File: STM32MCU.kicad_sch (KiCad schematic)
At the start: 17 parts, among them J7 Conn_02x05_Odd_Even, SW1 SW_Push, U4 STM32C542CCT6, Y1 ECS-120-18-33-JGN-TR

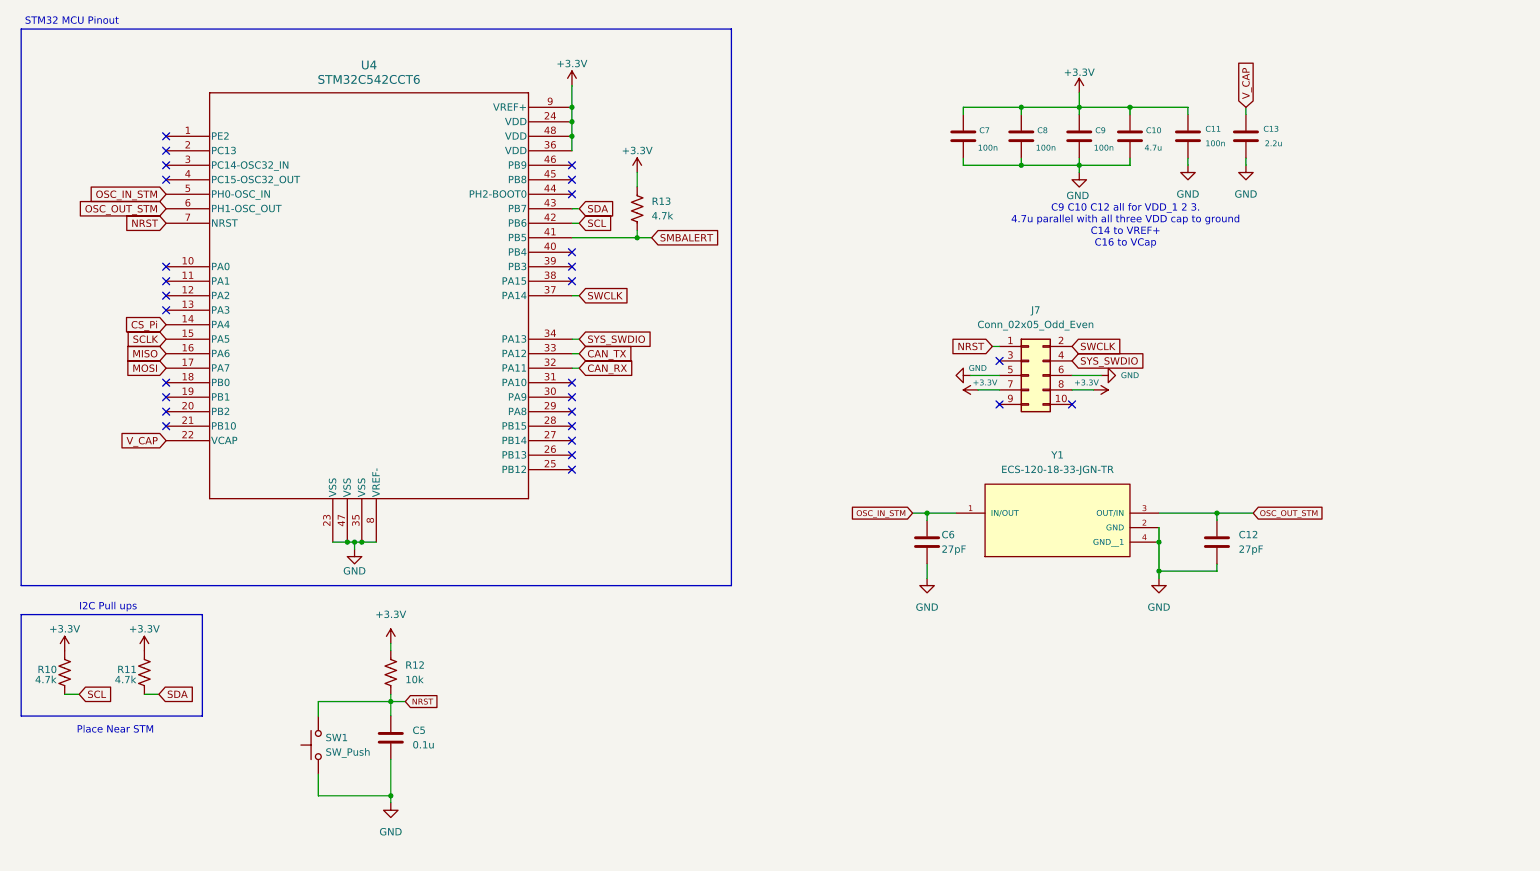
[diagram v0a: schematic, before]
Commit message: Split SMBALERT pins and added pull-up resistors
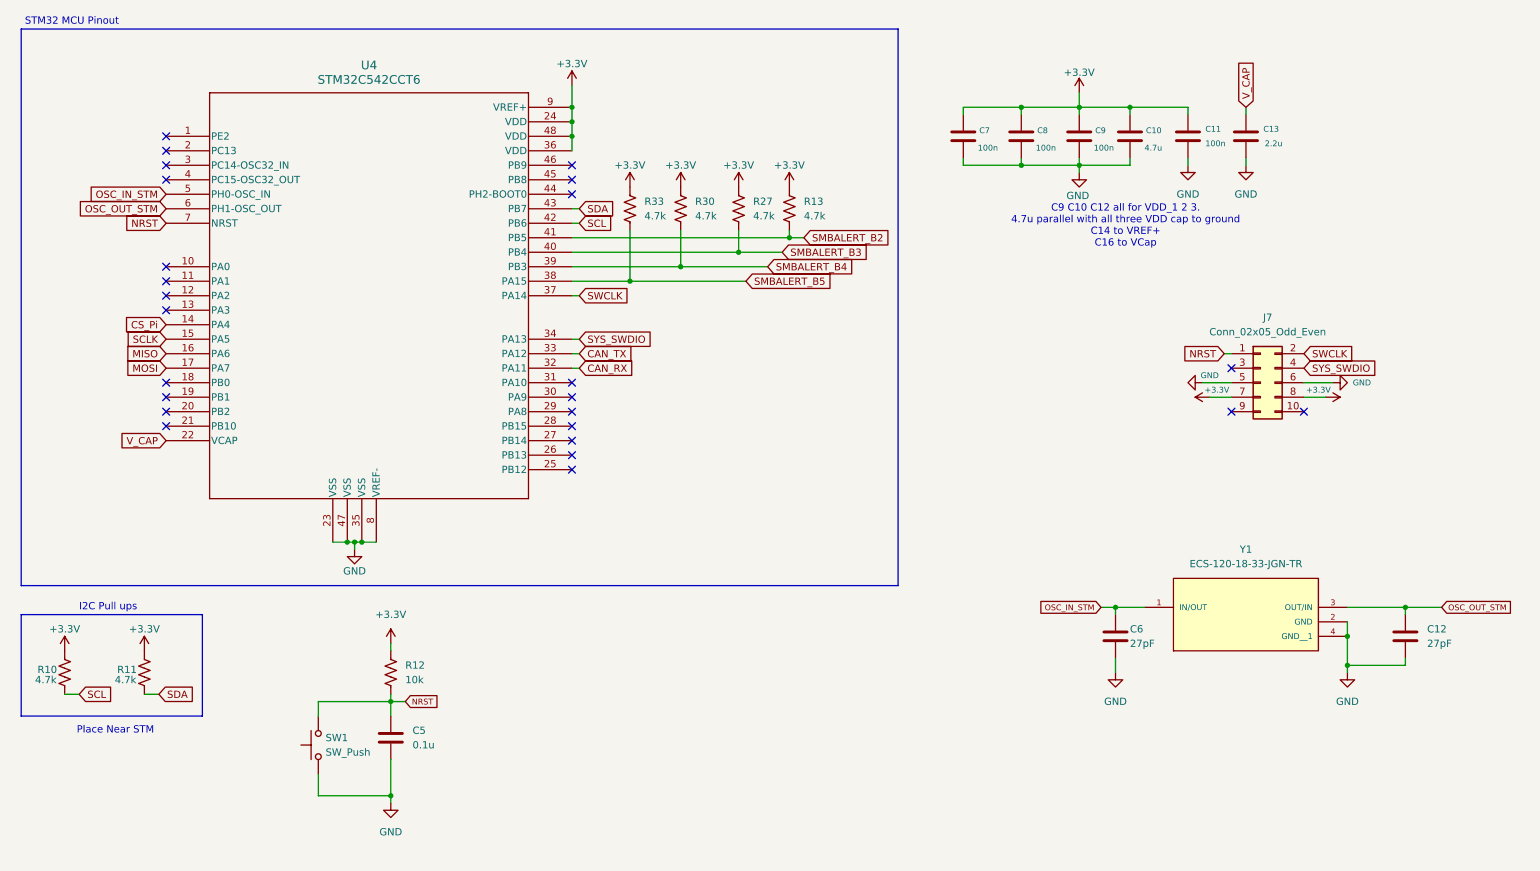
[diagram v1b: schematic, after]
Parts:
- added R27, R30, R33: 4.7k, E48SC12030NRFH, symbol Device:R_US
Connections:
- net +3.3V: now also R27.1, R30.1, R33.1
- net SMBALERT_B5: now reaches U4.38 (PA15)
- net SMBALERT_B5: now also R33.2
- net SMBALERT_B4: now reaches U4.39 (PB3)
- net SMBALERT_B4: now also R30.2
- net SMBALERT_B3: now reaches U4.40 (PB4)
- net SMBALERT_B3: now also R27.2
- net SMBALERT renamed SMBALERT_B2
- no-connect marks 28 -> 25
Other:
- moved on the sheet: C12, C6, J7, R13, Y1

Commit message: Added decouping caps
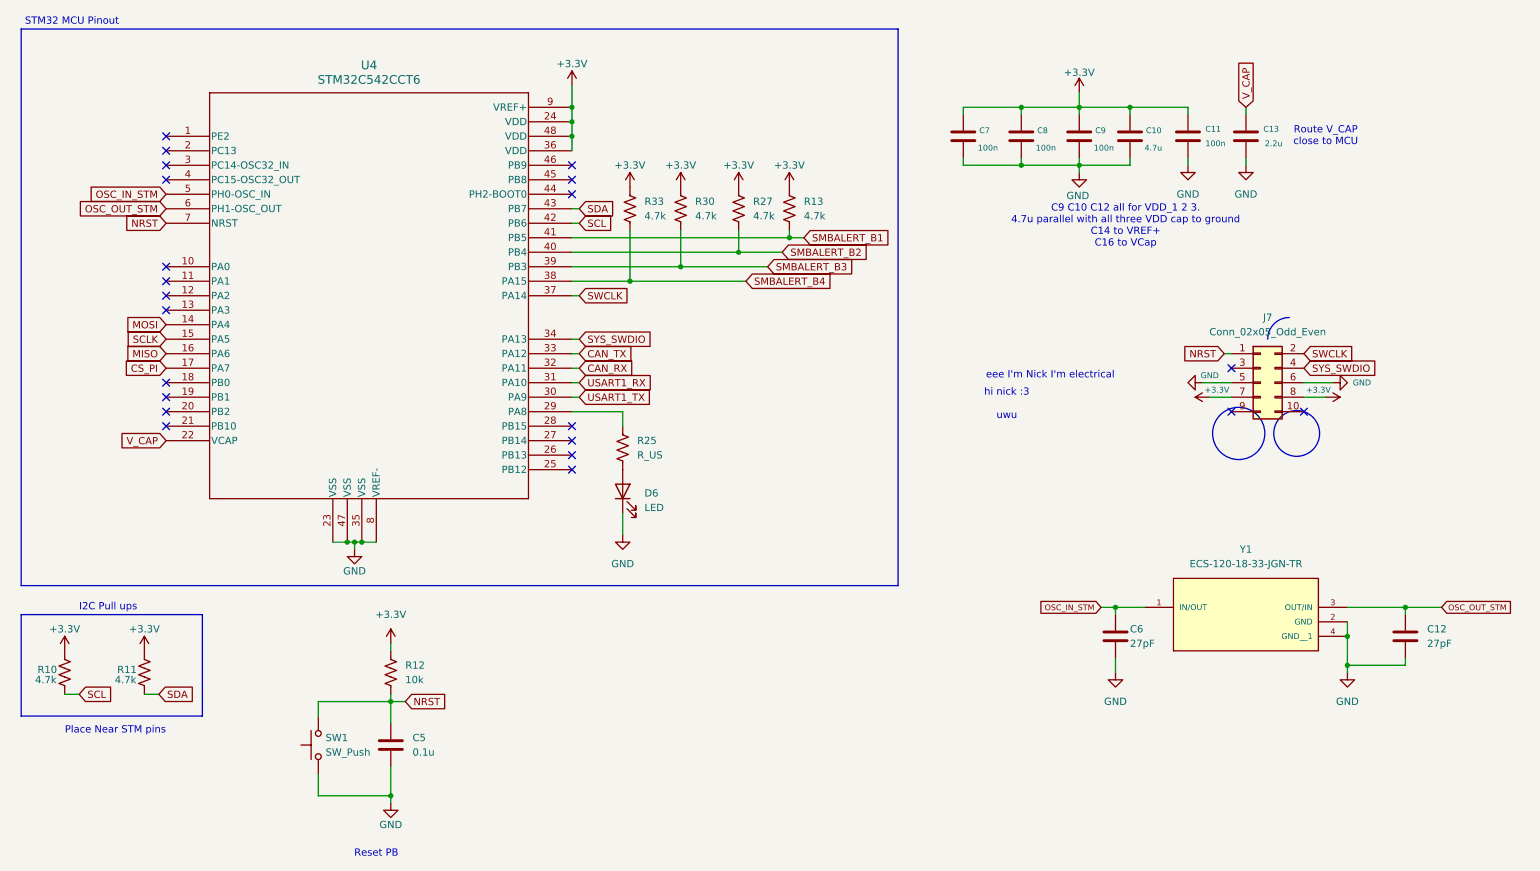
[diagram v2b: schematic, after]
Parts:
- added D6: LED, symbol Device:LED
- added R25: R_US, symbol Device:R_US
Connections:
- net CS_Pi is gone; now on net MOSI: U4.14 (PA4)
- net SMBALERT_B5 is gone; now on net SMBALERT_B4: R33.2, U4.38 (PA15)
- net GND: now also D6.1 (K)
- net MOSI: no longer U4.17 (PA7)
- net SMBALERT_B2: now also R27.2, U4.40 (PB4); no longer R13.2, U4.41 (PB5)
- net SMBALERT_B3: now also R30.2, U4.39 (PB3); no longer R27.2, U4.40 (PB4)
- net SMBALERT_B4: no longer R30.2, U4.39 (PB3)
- net at U4.29 (PA8): now also R25.1
- net USART1_TX: now reaches U4.30 (PA9)
- net USART1_RX: now reaches U4.31 (PA10)
- new net: D6.2 (A), R25.2
- new net CS_PI: U4.17 (PA7)
- new net SMBALERT_B1: R13.2, U4.41 (PB5)
- no-connect marks 25 -> 22
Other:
- note added: "Place Near STM pins"
- note added: "Reset PB"
- note added: "Route V_CAP close to MCU"
- note added: "eee I'm Nick I'm electrical"
- note added: "hi nick :3 uwu"
- note removed: "Place Near STM"
- moved on the sheet: C5

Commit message: Prettified, more power changes and MCU pin changes and removing redundancies
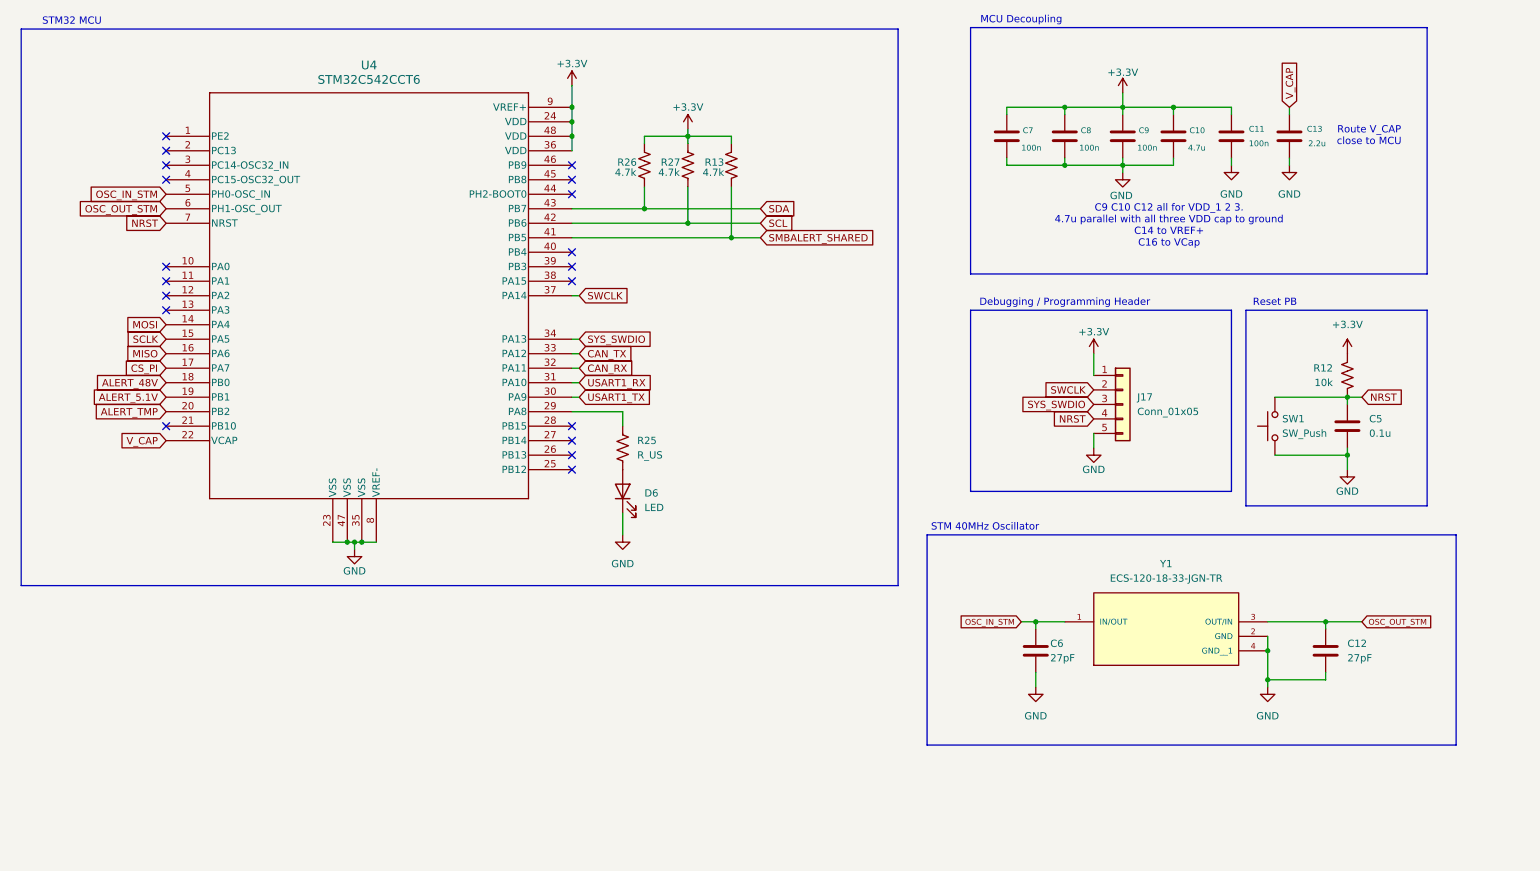
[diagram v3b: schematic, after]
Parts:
- removed J7: Conn_02x05_Odd_Even, Oscillator:Oscillator_SMD_ECS_2520MV-xxx-xx-4Pin_2.5x2.0mm, symbol Connector_Generic:Conn_02x05_Odd_Even
- removed R10, R11: 4.7k, symbol Device:R_US
- removed R30, R33: 4.7k, E48SC12030NRFH, symbol Device:R_US
- added J17: Conn_01x05, symbol Connector_Generic:Conn_01x05
- added R26: 4.7k, symbol Device:R_US
- R27: footprint E48SC12030NRFH -> (none)
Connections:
- net +3.3V: now also R27.2, J17.1 (Pin_1), R26.2; no longer R27.1
- net GND: now also J17.5 (Pin_5)
- net NRST: now also J17.4 (Pin_4)
- net SCL: now also R27.1
- net SDA: now also R26.1
- net SWCLK: now also J17.2 (Pin_2)
- net SYS_SWDIO: now also J17.3 (Pin_3)
- net ALERT_48V: now reaches U4.18 (PB0)
- net ALERT_5.1V: now reaches U4.19 (PB1)
- net ALERT_TMP: now reaches U4.20 (PB2)
- net SMBALERT_B1 renamed SMBALERT_SHARED
- net SMBALERT_B2: no longer names the net of U4.40 (PB4)
- net SMBALERT_B2: no longer R27.2
- net SMBALERT_B3: no longer names the net of U4.39 (PB3)
- net SMBALERT_B4: no longer names the net of U4.38 (PA15)
- no-connect marks 22 -> 19
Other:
- note added: "Debugging / Programming Header"
- note added: "MCU Decoupling"
- note added: "STM 40MHz Oscillator"
- note added: "STM32 MCU"
- note removed: "I2C Pull ups"
- note removed: "Place Near STM pins"
- note removed: "STM32 MCU Pinout"
- note removed: "eee I'm Nick I'm electrical"
- note removed: "hi nick :3 uwu"
- moved on the sheet: C10, C11, C12, C13, C5, C6, C7, C8, C9, R12, R13, SW1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

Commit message: Replaced improper brick with new one
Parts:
- renumbered C9 to C10, C10 to C11, C11 to C12, C12 to C14, C5 to C15, C6 to C8, C8 to C9, J17 to J14, R13 to R10, R12 to R11, R25 to R7, R26 to R8, R27 to R9, D6 to STM, U4 to U3
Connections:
- net ALERT_48V renamed INA_48V_ALERT_N
- net ALERT_5.1V renamed INA_5V1_ALERT_N
- net ALERT_TMP renamed TMP_ALERT_N

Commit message: Bennett TODOs
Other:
- note added: "Change to 16MHz osillator change capacitances to what is nededed check datasheet - Nick"
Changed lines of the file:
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@@
+		)
+	)
+	(text "Change to 16MHz osillator \n\nchange capacitances to what is nededed check datasheet\n\n- Nick"
+		(exclude_from_sim no)
+		(at 222.25 148.59 0)
+		(effects
+			(font
+				(size 1.27 1.27)
+				(color 255 0 13 1)
+			)
 		)
 	)

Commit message: updated some of nicks requested changes
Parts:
- removed STM: LED, symbol Device:LED
- removed Y1: ECS-120-18-33-JGN-TR, ECS-120-18-33-JGN-TR:XTAL_ECS-120-18-33-JGN-TR, symbol ECS-120-18-33-JGN-TR:ECS-120-18-33-JGN-TR
- added D6: WHAT COLOR, i6A4W_DIP_FULL_TDK, symbol Device:LED
- added Y1: ABM8G-16.000MHZ-18-D2Y-T, CRYSTAL_ABM8G_ABR, symbol 2026-10-14_21-13-20:ABM8G-16.000MHZ-18-D2Y-T
- R10: footprint E48SC12030NRFH -> rov_power:E48SC12030NRFH
- U3: footprint LQFP48-7X7 -> rov_logic:LQFP48-7X7
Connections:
- net GND: now also C14.1, D6.1 (K), Y1.2 (GND), Y1.4 (GND); no longer C14.2
- net OSC_IN_STM: now also Y1.1
- net OSC_OUT_STM: now also C14.2, Y1.3; no longer C14.1
- net at R7.2: now also D6.2 (A)
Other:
- moved on the sheet: C14, C8

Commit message: meeting notes and quick changes, someone needs to verify new components
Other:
- note added: "STM 16MHz Oscillator"
- note removed: "STM 40MHz Oscillator"
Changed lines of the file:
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@@
 		)
 	)
-	(text "STM 40MHz Oscillator"
+	(text "STM 16MHz Oscillator"
 		(exclude_from_sim no)
 		(at 187.96 104.14 0)

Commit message: assigned some cap and res footprints
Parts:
- C10, C12, C14, C15, C7, C8, C9: footprint (none) -> Capacitor_SMD:C_0603_1608Metric_Pad1.08x0.95mm_HandSolder
- C11, C13: footprint (none) -> Capacitor_SMD:C_1206_3216Metric_Pad1.33x1.80mm_HandSolder
- D6: footprint i6A4W_DIP_FULL_TDK -> LED_SMD:LED_0805_2012Metric_Pad1.15x1.40mm_HandSolder
- J14: footprint (none) -> Connector_PinHeader_2.54mm:PinHeader_1x05_P2.54mm_Vertical
- R10: footprint rov_power:E48SC12030NRFH -> Resistor_SMD:R_0603_1608Metric_Pad0.98x0.95mm_HandSolder
- R7, R8, R9: footprint (none) -> Resistor_SMD:R_0603_1608Metric_Pad0.98x0.95mm_HandSolder
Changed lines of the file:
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@@
 			)
 		)
-		(property "Footprint" ""
+		(property "Footprint" "Capacitor_SMD:C_0603_1608Metric_Pad1.08x0.95mm_HandSolder"
 			(at 202.8952 39.37 0)
 			(hide yes)
@@
 			)
 		)
-		(property "Footprint" ""
+		(property "Footprint" "Capacitor_SMD:C_1206_3216Metric_Pad1.33x1.80mm_HandSolder"
 			(at 242.2652 39.37 0)
 			(hide yes)
@@
 			)
 		)
-		(property "Footprint" ""
+		(property "Footprint" "Resistor_SMD:R_0603_1608Metric_Pad0.98x0.95mm_HandSolder"
 			(at 134.874 40.386 90)
 			(hide yes)
@@
 			)
 		)
-		(property "Footprint" ""
+		(property "Footprint" "Connector_PinHeader_2.54mm:PinHeader_1x05_P2.54mm_Vertical"
 			(at 212.09 82.55 0)
 			(hide yes)
@@
 			)
 		)
-		(property "Footprint" ""
+		(property "Footprint" "Capacitor_SMD:C_0603_1608Metric_Pad1.08x0.95mm_HandSolder"
 			(at 200.9648 118.11 0)
 			(hide yes)
@@
 			)
 		)
-		(property "Footprint" ""
+		(property "Footprint" "Capacitor_SMD:C_0603_1608Metric_Pad1.08x0.95mm_HandSolder"
 			(at 213.0552 39.37 0)
 			(hide yes)
@@
 			)
 		)
-		(property "Footprint" ""
+		(property "Footprint" "Resistor_SMD:R_0603_1608Metric_Pad0.98x0.95mm_HandSolder"
 			(at 127.254 40.386 90)
 			(hide yes)
@@
 			)
 		)
-		(property "Footprint" "rov_power:E48SC12030NRFH"
+		(property "Footprint" "Resistor_SMD:R_0603_1608Metric_Pad0.98x0.95mm_HandSolder"
 			(at 142.494 40.894 90)
 			(hide yes)
@@
 			)
 		)
-		(property "Footprint" ""
+		(property "Footprint" "Capacitor_SMD:C_0603_1608Metric_Pad1.08x0.95mm_HandSolder"
 			(at 232.1052 39.37 0)
 			(hide yes)
@@
 			)
 		)
-		(property "Footprint" ""
+		(property "Footprint" "Capacitor_SMD:C_1206_3216Metric_Pad1.33x1.80mm_HandSolder"
 			(at 221.9452 39.37 0)
 			(hide yes)
@@
 			)
 		)
-		(property "Footprint" "i6A4W_DIP_FULL_TDK"
+		(property "Footprint" "LED_SMD:LED_0805_2012Metric_Pad1.15x1.40mm_HandSolder"
 			(at 124.46 97.79 0)
 			(hide yes)
@@
 			)
 		)
-		(property "Footprint" ""
+		(property "Footprint" "Resistor_SMD:R_0603_1608Metric_Pad0.98x0.95mm_HandSolder"
 			(at 125.476 90.424 90)
 			(hide yes)
@@
 			)
 		)
-		(property "Footprint" ""
+		(property "Footprint" "Capacitor_SMD:C_0603_1608Metric_Pad1.08x0.95mm_HandSolder"
 			(at 256.2352 125.73 0)
 			(hide yes)
@@
 			)
 		)
-		(property "Footprint" ""
+		(property "Footprint" "Capacitor_SMD:C_0603_1608Metric_Pad1.08x0.95mm_HandSolder"
 			(at 192.7352 39.37 0)
 			(hide yes)
@@
 			)
 		)
-		(property "Footprint" ""
+		(property "Footprint" "Capacitor_SMD:C_0603_1608Metric_Pad1.08x0.95mm_HandSolder"
 			(at 252.4252 90.17 0)
 			(hide yes)
